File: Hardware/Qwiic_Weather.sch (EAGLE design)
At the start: 25 parts, among them J1 QWIIC, J2 QWIIC, J3 PTH, U1 BME280

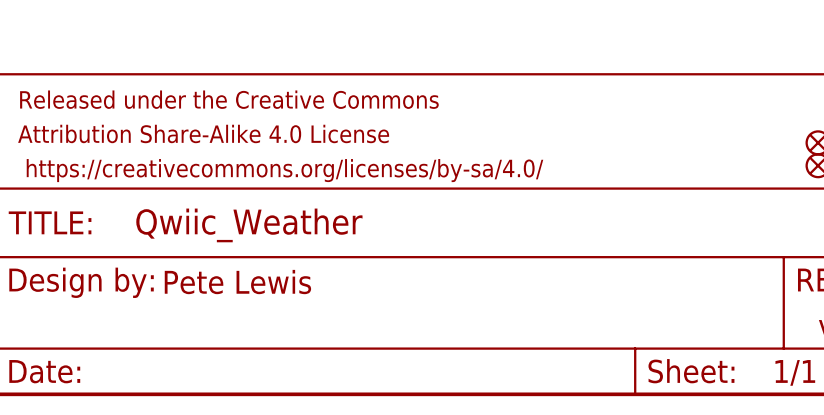
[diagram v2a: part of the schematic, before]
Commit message: Finished Layout
Finished Routing and Added pin and jumper labels.
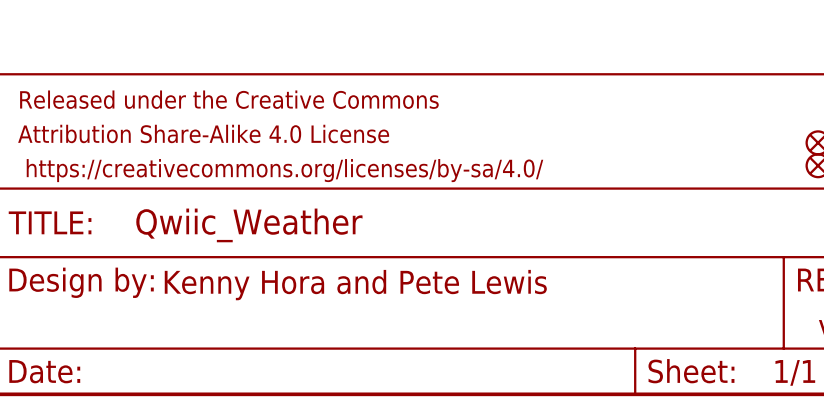
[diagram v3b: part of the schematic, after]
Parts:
- SJ3: device SparkFun-Passives:JUMPER-PAD-3-2OF3_NC_BY_TRACE_SMALL -> SparkFun-Jumpers:JUMPER-SMT_3_1-NC_TRACE_NO-SILK
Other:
- note added: "Kenny Hora and Pete Lewis"
- note removed: "Pete Lewis"
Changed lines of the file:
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@@
 <grid distance="0.1" unitdist="inch" unit="inch" style="lines" multiple="1" display="no" altdistance="0.01" altunitdist="inch" altunit="inch"/>
 <layers>
-<layer number="1" name="Top" color="4" fill="1" visible="no" active="no"/>
-<layer number="2" name="Route2" color="1" fill="3" visible="no" active="no"/>
-<layer number="3" name="Route3" color="4" fill="3" visible="no" active="no"/>
-<layer number="4" name="Route4" color="1" fill="4" visible="no" active="no"/>
-<layer number="5" name="Route5" color="4" fill="4" visible="no" active="no"/>
-<layer number="6" name="Route6" color="1" fill="8" visible="no" active="no"/>
-<layer number="7" name="Route7" color="4" fill="8" visible="no" active="no"/>
-<layer number="8" name="Route8" color="1" fill="2" visible="no" active="no"/>
-<layer number="9" name="Route9" color="4" fill="2" visible="no" active="no"/>
-<layer number="10" name="Route10" color="1" fill="7" visible="no" active="no"/>
-<layer number="11" name="Route11" color="4" fill="7" visible="no" active="no"/>
-<layer number="12" name="Route12" color="1" fill="5" visible="no" active="no"/>
-<layer number="13" name="Route13" color="4" fill="5" visible="no" active="no"/>
-<layer number="14" name="Route14" color="1" fill="6" visible="no" active="no"/>
-<layer number="15" name="Route15" color="4" fill="6" visible="no" active="no"/>
-<layer number="16" name="Bottom" color="1" fill="1" visible="no" active="no"/>
-<layer number="17" name="Pads" color="2" fill="1" visible="no" active="no"/>
-<layer number="18" name="Vias" color="2" fill="1" visible="no" active="no"/>
-<layer number="19" name="Unrouted" color="6" fill="1" visible="no" active="no"/>
-<layer number="20" name="Dimension" color="24" fill="1" visible="no" active="no"/>
-<layer number="21" name="tPlace" color="16" fill="1" visible="no" active="no"/>
-<layer number="22" name="bPlace" color="14" fill="1" visible="no" active="no"/>
-<layer number="23" name="tOrigins" color="15" fill="1" visible="no" active="no"/>
-<layer number="24" name="bOrigins" color="15" fill="1" visible="no" active="no"/>
-<layer number="25" name="tNames" color="7" fill="1" visible="no" active="no"/>
-<layer number="26" name="bNames" color="7" fill="1" visible="no" active="no"/>
-<layer number="27" name="tValues" color="7" fill="1" visible="no" active="no"/>
-<layer number="28" name="bValues" color="7" fill="1" visible="no" active="no"/>
+<layer number="1" name="Top" color="4" fill="1" visible="yes" active="no"/>
+<layer number="2" name="Route2" color="1" fill="3" visible="yes" active="no"/>
+<layer number="3" name="Route3" color="4" fill="3" visible="yes" active="no"/>
+<layer number="4" name="Route4" color="1" fill="4" visible="yes" active="no"/>
+<layer number="5" name="Route5" color="4" fill="4" visible="yes" active="no"/>
+<layer number="6" name="Route6" color="1" fill="8" visible="yes" active="no"/>
+<layer number="7" name="Route7" color="4" fill="8" visible="yes" active="no"/>
+<layer number="8" name="Route8" color="1" fill="2" visible="yes" active="no"/>
+<layer number="9" name="Route9" color="4" fill="2" visible="yes" active="no"/>
+<layer number="10" name="Route10" color="1" fill="7" visible="yes" active="no"/>
+<layer number="11" name="Route11" color="4" fill="7" visible="yes" active="no"/>
+<layer number="12" name="Route12" color="1" fill="5" visible="yes" active="no"/>
+<layer number="13" name="Route13" color="4" fill="5" visible="yes" active="no"/>
+<layer number="14" name="Route14" color="1" fill="6" visible="yes" active="no"/>
+<layer number="15" name="Route15" color="4" fill="6" visible="yes" active="no"/>
+<layer number="16" name="Bottom" color="1" fill="1" visible="yes" active="no"/>
+<layer number="17" name="Pads" color="2" fill="1" visible="yes" active="no"/>
+<layer number="18" name="Vias" color="2" fill="1" visible="yes" active="no"/>
+<layer number="19" name="Unrouted" color="6" fill="1" visible="yes" active="no"/>
+<layer number="20" name="Dimension" color="24" fill="1" visible="yes" active="no"/>
+<layer number="21" name="tPlace" color="16" fill="1" visible="yes" active="no"/>
+<layer number="22" name="bPlace" color="14" fill="1" visible="yes" active="no"/>
+<layer number="23" name="tOrigins" color="15" fill="1" visible="yes" active="no"/>
+<layer number="24" name="bOrigins" color="15" fill="1" visible="yes" active="no"/>
+<layer number="25" name="tNames" color="7" fill="1" visible="yes" active="no"/>
+<layer number="26" name="bNames" color="7" fill="1" visible="yes" active="no"/>
+<layer number="27" name="tValues" color="7" fill="1" visible="yes" active="no"/>
+<layer number="28" name="bValues" color="7" fill="1" visible="yes" active="no"/>
 <layer number="29" name="tStop" color="7" fill="3" visible="no" active="no"/>
 <layer number="30" name="bStop" color="7" fill="6" visible="no" active="no"/>
@@
 <layer number="35" name="tGlue" color="7" fill="4" visible="no" active="no"/>
 <layer number="36" name="bGlue" color="7" fill="5" visible="no" active="no"/>
-<layer number="37" name="tTest" color="7" fill="1" visible="no" active="no"/>
-<layer number="38" name="bTest" color="7" fill="1" visible="no" active="no"/>
+<layer number="37" name="tTest" color="7" fill="1" visible="yes" active="no"/>
+<layer number="38" name="bTest" color="7" fill="1" visible="yes" active="no"/>
 <layer number="39" name="tKeepout" color="4" fill="11" visible="no" active="no"/>
 <layer number="40" name="bKeepout" color="1" fill="11" visible="no" active="no"/>
@@
 <layer number="44" name="Drills" color="7" fill="1" visible="no" active="no"/>
 <layer number="45" name="Holes" color="7" fill="1" visible="no" active="no"/>
-<layer number="46" name="Milling" color="3" fill="1" visible="no" active="no"/>
-<layer number="47" name="Measures" color="7" fill="1" visible="no" active="no"/>
-<layer number="48" name="Document" color="7" fill="1" visible="no" active="no"/>
-<layer number="49" name="Reference" color="7" fill="1" visible="no" active="no"/>
-<layer number="50" name="dxf" color="7" fill="1" visible="no" active="no"/>
-<layer number="51" name="tDocu" color="6" fill="1" visible="no" active="no"/>
-<layer number="52" name="bDocu" color="7" fill="1" visible="no" active="no"/>
-<layer number="53" name="tGND_GNDA" color="7" fill="9" visible="no" active="no"/>
-<layer number="54" name="bGND_GNDA" color="1" fill="9" visible="no" active="no"/>
-<layer number="56" name="wert" color="7" fill="1" visible="no" active="no"/>
-<layer number="57" name="tCAD" color="7" fill="1" visible="no" active="no"/>
-<layer number="59" name="tCarbon" color="7" fill="1" visible="no" active="no"/>
-<layer number="60" name="bCarbon" color="7" fill="1" visible="no" active="no"/>
+<layer number="46" name="Milling" color="3" fill="1" visible="yes" active="no"/>
+<layer number="47" name="Measures" color="7" fill="1" visible="yes" active="no"/>
+<layer number="48" name="Document" color="7" fill="1" visible="yes" active="no"/>
+<layer number="49" name="Reference" color="7" fill="1" visible="yes" active="no"/>
+<layer number="50" name="dxf" color="7" fill="1" visible="yes" active="no"/>
+<layer number="51" name="tDocu" color="6" fill="1" visible="yes" active="no"/>
+<layer number="52" name="bDocu" color="7" fill="1" visible="yes" active="no"/>
+<layer number="53" name="tGND_GNDA" color="7" fill="9" visible="yes" active="no"/>
+<layer number="54" name="bGND_GNDA" color="1" fill="9" visible="yes" active="no"/>
+<layer number="56" name="wert" color="7" fill="1" visible="yes" active="no"/>
+<layer number="57" name="tCAD" color="7" fill="1" visible="yes" active="no"/>
+<layer number="59" name="tCarbon" color="7" fill="1" visible="yes" active="no"/>
+<layer number="60" name="bCarbon" color="7" fill="1" visible="yes" active="no"/>
 <layer number="88" name="SimResults" color="9" fill="1" visible="no" active="yes"/>
 <layer number="89" name="SimProbes" color="9" fill="1" visible="no" active="yes"/>
@@
 <part name="SJ2" library="SparkFun-Passives" deviceset="JUMPER-PAD-2-NC_BY_TRACE" device="" value="EN I2C MODE"/>
 <part name="SUPPLY3" library="SparkFun-Aesthetics" deviceset="3.3V" device=""/>
-<part name="SJ3" library="SparkFun-Passives" deviceset="JUMPER-PAD-3-2OF3_NC_BY_TRACE" device="_SMALL" value="EN ADR PU"/>
+<part name="SJ3" library="SparkFun-Jumpers" deviceset="JUMPER-SMT_3_1-NC_TRACE" device="_NO-SILK" value="EN ADR PU"/>
 <part name="R2" library="SparkFun-Resistors" deviceset="4.7KOHM-1/10W-1%(0603)" device="" value="4.7K"/>
 <part name="SUPPLY5" library="SparkFun-Aesthetics" deviceset="3.3V" device=""/>
@@
 resistors.</text>
 <text x="238.76" y="7.62" size="2.54" layer="94" font="vector" align="center-left">v10</text>
-<text x="165.862" y="11.176" size="2.54" layer="94" font="vector">Pete Lewis</text>
+<text x="165.862" y="11.176" size="2.54" layer="94" font="vector">Kenny Hora and Pete Lewis</text>
 <wire x1="248.92" y1="83.82" x2="0" y2="83.82" width="0.2032" layer="97" style="longdash"/>
 <text x="135.636" y="140.208" size="1.778" layer="97" align="top-left">DEFAULT: I2C mode</text>

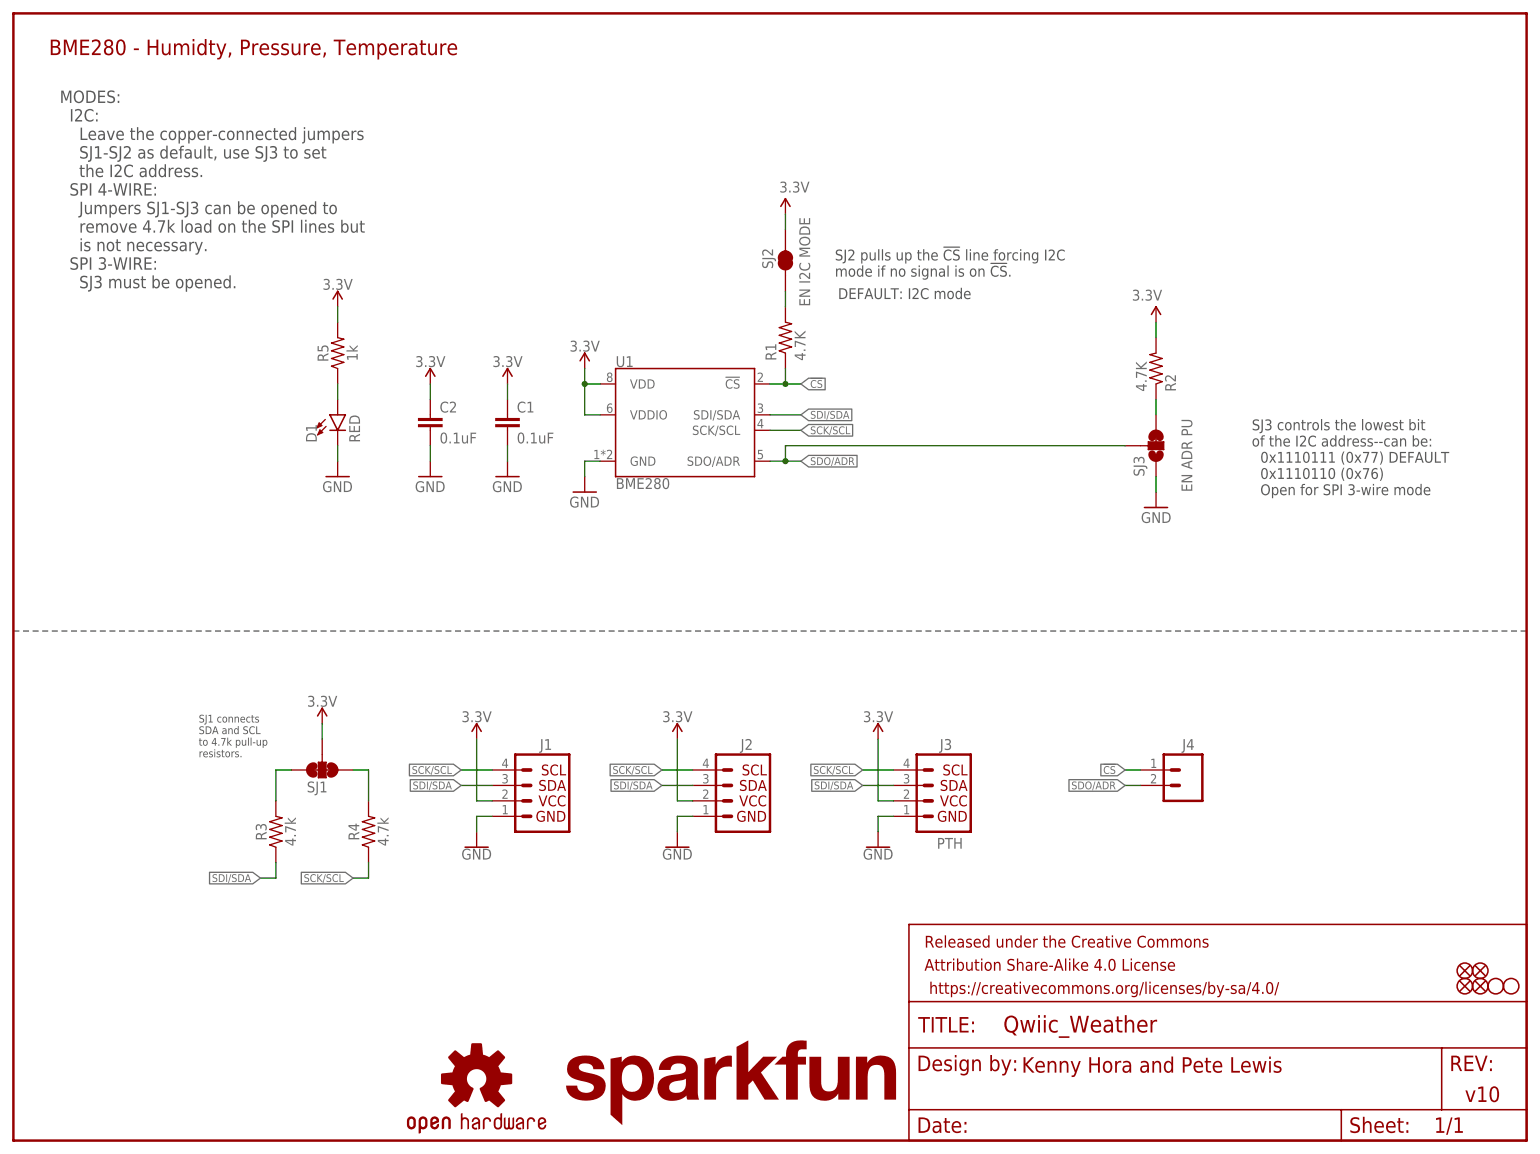
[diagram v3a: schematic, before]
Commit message: layout and library update work
-updated 4.7K resistors to newest device (no silk under part).
-removed some unncessary vis on 3.3V net, and rerouted.
-nudges some traces and power LED for more efficient routing and better GND flow.
-Moved Jumpers to no silk packages (for consistency)
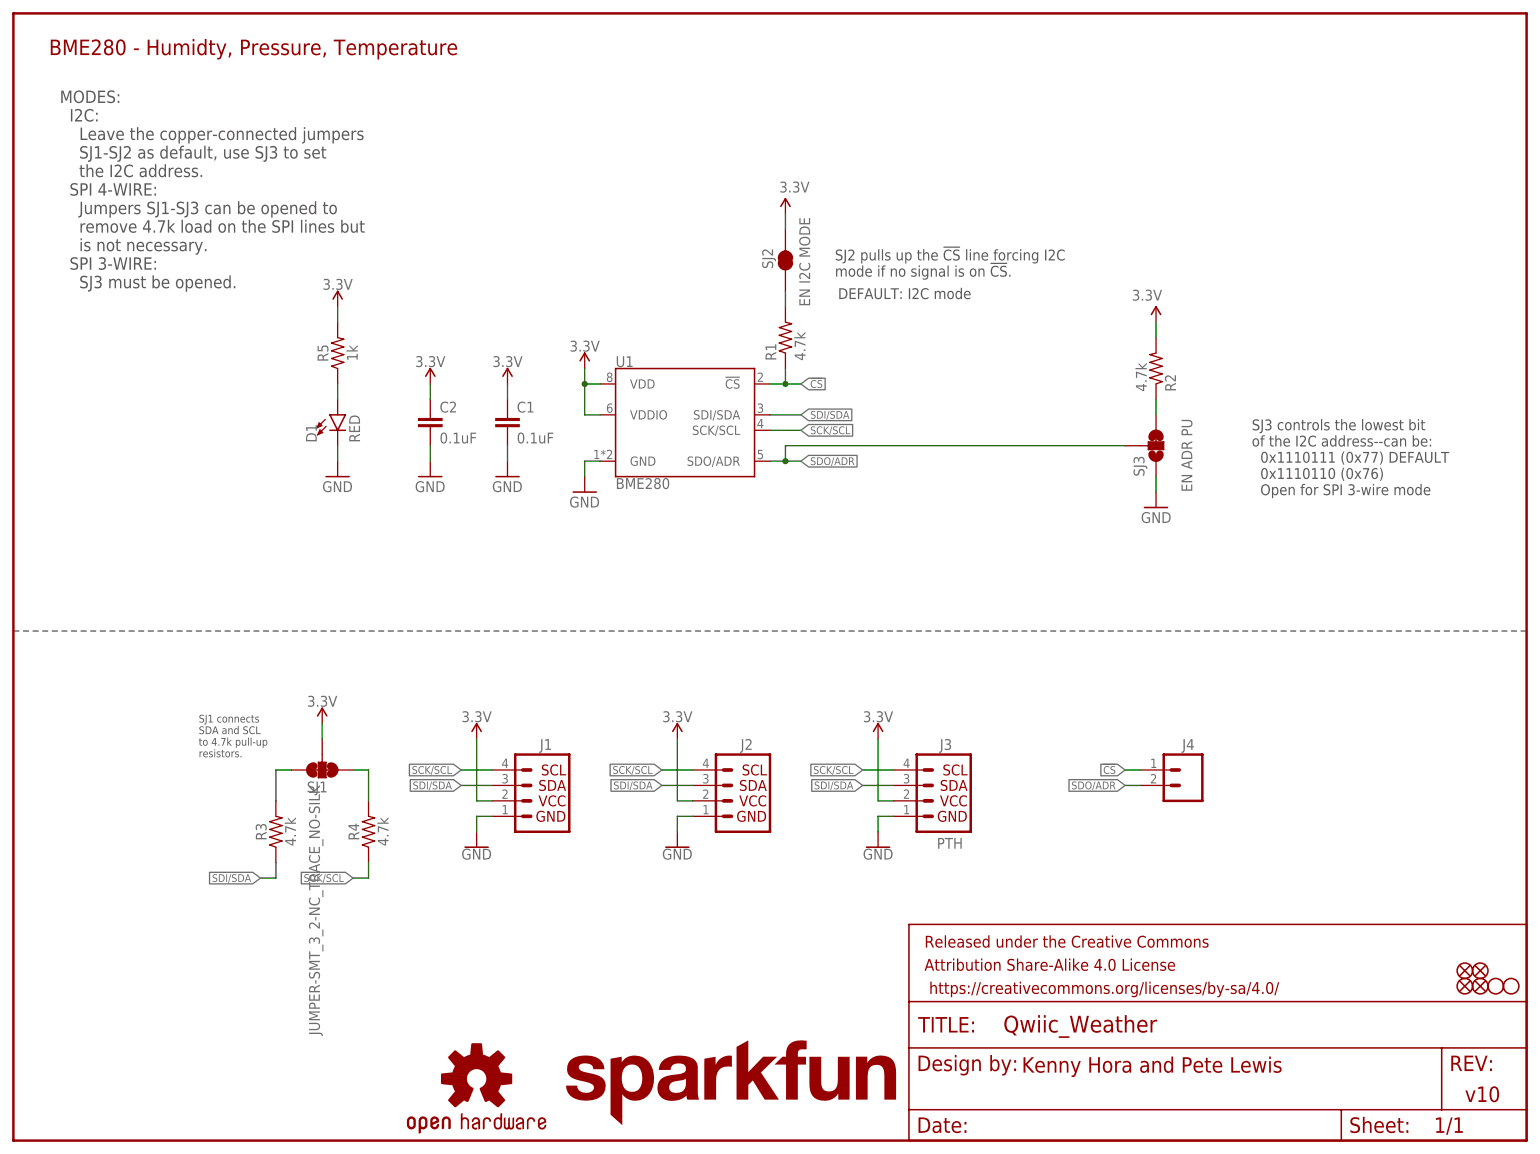
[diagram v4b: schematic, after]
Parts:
- R1, R2: value 4.7K -> 4.7k; device SparkFun-Resistors:4.7KOHM-1/10W-1%(0603) -> SparkFun-Resistors:4.7KOHM-0603-1/10W-1%
- SJ1: value JUMPER-SMT_3_2-NC_TRACE_SILK -> JUMPER-SMT_3_2-NC_TRACE_NO-SILK; device SparkFun-Jumpers:JUMPER-SMT_3_2-NC_TRACE_SILK -> SparkFun-Jumpers:JUMPER-SMT_3_2-NC_TRACE_NO-SILK
- SJ2: device SparkFun-Passives:JUMPER-PAD-2-NC_BY_TRACE -> SparkFun-Passives:JUMPER-PAD-2-NC_BY_TRACENO_SILK
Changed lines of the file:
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@@
 <?xml version="1.0" encoding="utf-8"?>
 <!DOCTYPE eagle SYSTEM "eagle.dtd">
-<eagle version="9.4.2">
+<eagle version="9.4.0">
 <drawing>
 <settings>
@@
 <part name="H4" library="SparkFun-Hardware" deviceset="STAND-OFF" device=""/>
 <part name="H2" library="SparkFun-Hardware" deviceset="STAND-OFF" device=""/>
-<part name="SJ1" library="SparkFun-Jumpers" deviceset="JUMPER-SMT_3_2-NC_TRACE" device="_SILK" value=""/>
+<part name="SJ1" library="SparkFun-Jumpers" deviceset="JUMPER-SMT_3_2-NC_TRACE" device="_NO-SILK" value="JUMPER-SMT_3_2-NC_TRACE_NO-SILK"/>
 <part name="LOGO4" library="SparkFun-Aesthetics" deviceset="OSHW-LOGO" device="S"/>
 <part name="FD1" library="SparkFun-Aesthetics" deviceset="FIDUCIAL" device="1X2"/>
@@
 <part name="C2" library="SparkFun-Capacitors" deviceset="0.1UF" device="-0603-25V-(+80/-20%)" value="0.1uF"/>
 <part name="SUPPLY2" library="SparkFun-PowerSymbols" deviceset="3.3V" device=""/>
-<part name="R1" library="SparkFun-Resistors" deviceset="4.7KOHM-1/10W-1%(0603)" device="" value="4.7K"/>
-<part name="SJ2" library="SparkFun-Passives" deviceset="JUMPER-PAD-2-NC_BY_TRACE" device="" value="EN I2C MODE"/>
+<part name="R1" library="SparkFun-Resistors" deviceset="4.7KOHM" device="-0603-1/10W-1%" value="4.7k"/>
+<part name="SJ2" library="SparkFun-Passives" deviceset="JUMPER-PAD-2-NC_BY_TRACE" device="NO_SILK" value="EN I2C MODE"/>
 <part name="SUPPLY3" library="SparkFun-Aesthetics" deviceset="3.3V" device=""/>
 <part name="SJ3" library="SparkFun-Jumpers" deviceset="JUMPER-SMT_3_1-NC_TRACE" device="_NO-SILK" value="EN ADR PU"/>
-<part name="R2" library="SparkFun-Resistors" deviceset="4.7KOHM-1/10W-1%(0603)" device="" value="4.7K"/>
+<part name="R2" library="SparkFun-Resistors" deviceset="4.7KOHM" device="-0603-1/10W-1%" value="4.7k"/>
 <part name="SUPPLY5" library="SparkFun-Aesthetics" deviceset="3.3V" device=""/>
 <part name="GND5" library="SparkFun-Aesthetics" deviceset="GND" device=""/>
